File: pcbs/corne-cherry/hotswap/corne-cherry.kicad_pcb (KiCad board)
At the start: 2 copper layers, 277.2 x 107.5 mm, 190 parts, among them J1 TYPE-C-31-M-13C, J2 TRS, J3 Conn_01x04, J4 Conn_01x03, SW1 SW_Push, SW10 SW_Push, SW11 SW_Push, SW12 SW_Push, SW13 SW_Push, SW14 SW_Push, SW15 SW_Push, SW16 SW_Push, SW17 SW_Push, SW18 SW_Push, SW19 SW_Push, SW2 SW_Push, SW20 SW_Push, SW21 SW_Push, SW22 SW_Push, SW23 SW_Push, SW24 SW_Push, SW3 SW_Push, SW4 SW_Push, SW5 SW_Push, SW6 SW_Push, SW7 SW_Push, SW8 SW_Push, SW9 SW_Push, U1 RP2040, U2 NCP1117LPST33T3G, U3 TPD4E05U06DQAR, U4 W25Q128JVSIQ, Y1 12MHz 18pF

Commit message: logo
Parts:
- added G***: LOGO, kbd_local:corne-logo-horizontal, F.Cu at (305.7, -77.0)
- added G***: LOGO, kbd_local:corne-logo-horizontal, F.Cu at (124.7, -77.0)

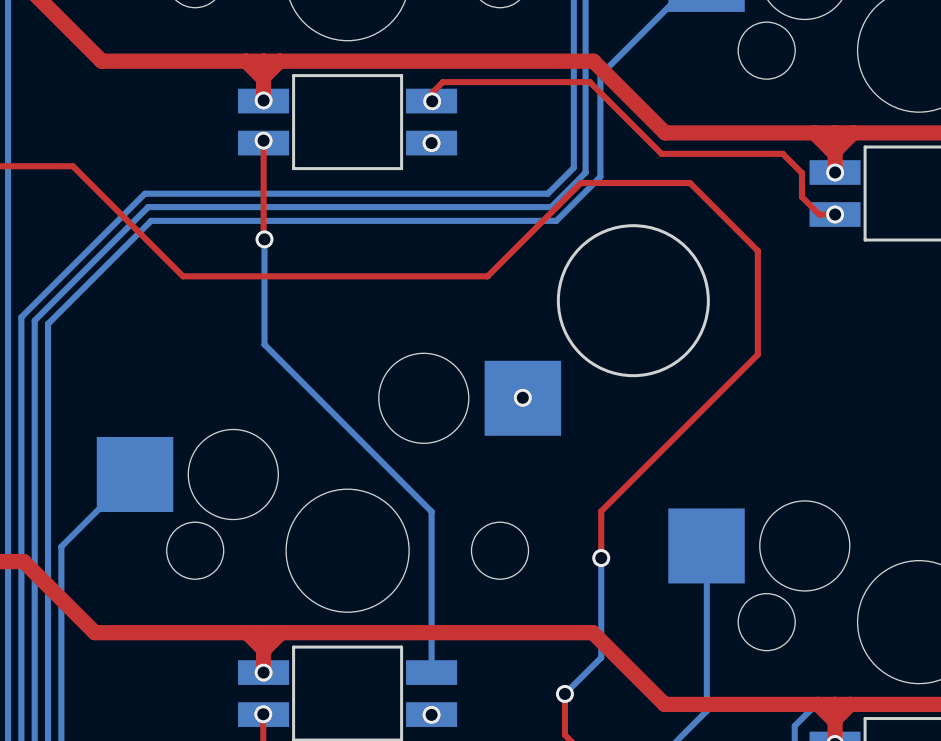
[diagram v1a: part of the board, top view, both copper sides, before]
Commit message: fixed left LED5 wiring issue
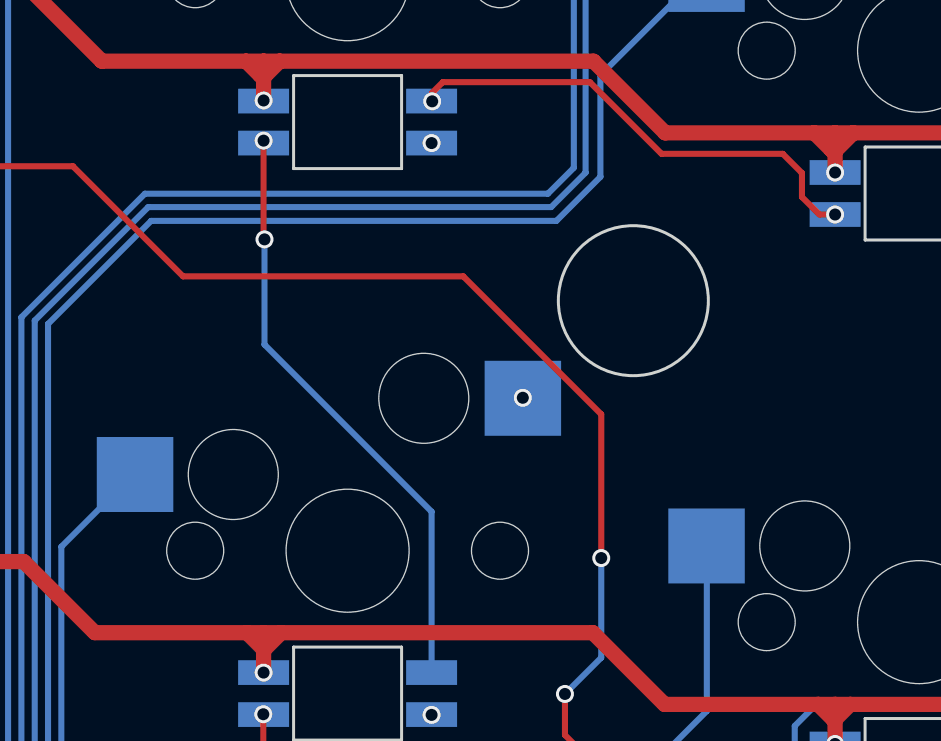
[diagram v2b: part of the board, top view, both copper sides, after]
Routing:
- net /left/KEY22: track 272.7 -> 259.5 mm
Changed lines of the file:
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@@
 	)
 	(segment
-		(start 174.252502 -121.10875)
-		(end 176.512502 -118.84875)
+		(start 166.692502 -117.99875)
+		(end 171.292502 -113.39875)
 		(width 0.2032)
 		(layer "F.Cu")
@@
 	)
 	(segment
-		(start 170.612502 -121.10875)
-		(end 174.252502 -121.10875)
-		(width 0.2032)
-		(layer "F.Cu")
-		(net 30)
-	)
-	(segment
-		(start 176.512502 -115.38875)
-		(end 171.292502 -110.16875)
-		(width 0.2032)
-		(layer "F.Cu")
-		(net 30)
-	)
-	(segment
-		(start 167.502502 -117.99875)
-		(end 170.612502 -121.10875)
+		(start 171.292502 -113.39875)
+		(end 171.292502 -108.60875)
 		(width 0.2032)
 		(layer "F.Cu")
@@
 	)
 	(segment
-		(start 171.292502 -110.16875)
-		(end 171.292502 -108.60875)
-		(width 0.2032)
-		(layer "F.Cu")
-		(net 30)
-	)
-	(segment
 		(start 77.382502 -110.23875)
 		(end 80.072502 -112.92875)
@@
 	)
 	(segment
-		(start 176.512502 -118.84875)
-		(end 176.512502 -115.38875)
-		(width 0.2032)
-		(layer "F.Cu")
-		(net 30)
-	)
-	(segment
 		(start 193.9375 -121.083352)
 		(end 193.9375 -118.537202)
@@
 	(segment
 		(start 157.352502 -117.99875)
-		(end 167.502502 -117.99875)
+		(end 166.692502 -117.99875)
 		(width 0.2032)
 		(layer "F.Cu")
